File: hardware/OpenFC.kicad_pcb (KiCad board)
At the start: 6 copper layers, 37.5 x 37.5 mm, 167 parts, among them J1 5V, J13 5V, J14 5V, J15 5V, J16 5V, J17 5V, J18 5V, J19 5V, J2 5V, J20 5V, J21 5V, J22 5V, J23 5V, J24 5V, J25 5V, J27 5V, J28 5V, J29 5V, J3 5V, J30 5V, J32 5V, J33 5V, J34 5V, J35 5V, J36 5V, J38 5V, J39 5V, J4 5V, J40 5V, J41 5V, J42 5V, J43 5V, J44 5V, J45 5V, J46 5V, J47 5V, J48 5V, J49 5V, J5 5V, J50 5V, J51 5V, J52 5V, J53 5V, J54 5V, J55 5V, J56 5V, J57 5V, J58 5V, J59 5V, J6 5V, J7 5V, J8 5V, J9 5V, P1 SM08B-SRSS-TB(LF)(SN), Q1 DMN1150UFB-7B, Q2 DMN1150UFB-7B, Q3 DMN1150UFB-7B, Q7 DMN1150UFB-7B, U1 SM06B-SRSS-TB(LF)(SN), U13 LP5912-3.3DRVR, U14 LSM6DSV16XTR, U21 NCV8187AMT180TAG, U32 TS2306A 240GF MSM 9_C2976675, U33 TPS2116DRLR, U34 TLV3201AIDBVR, U35 SN74LVC1G3157DTBR, U36 RP2354B_C39843328, U38 TLV9061IDPWR, U6 LMR51420YFDDCR, U7 LMR51420YFDDCR, X1 XTM25012000JT00351001

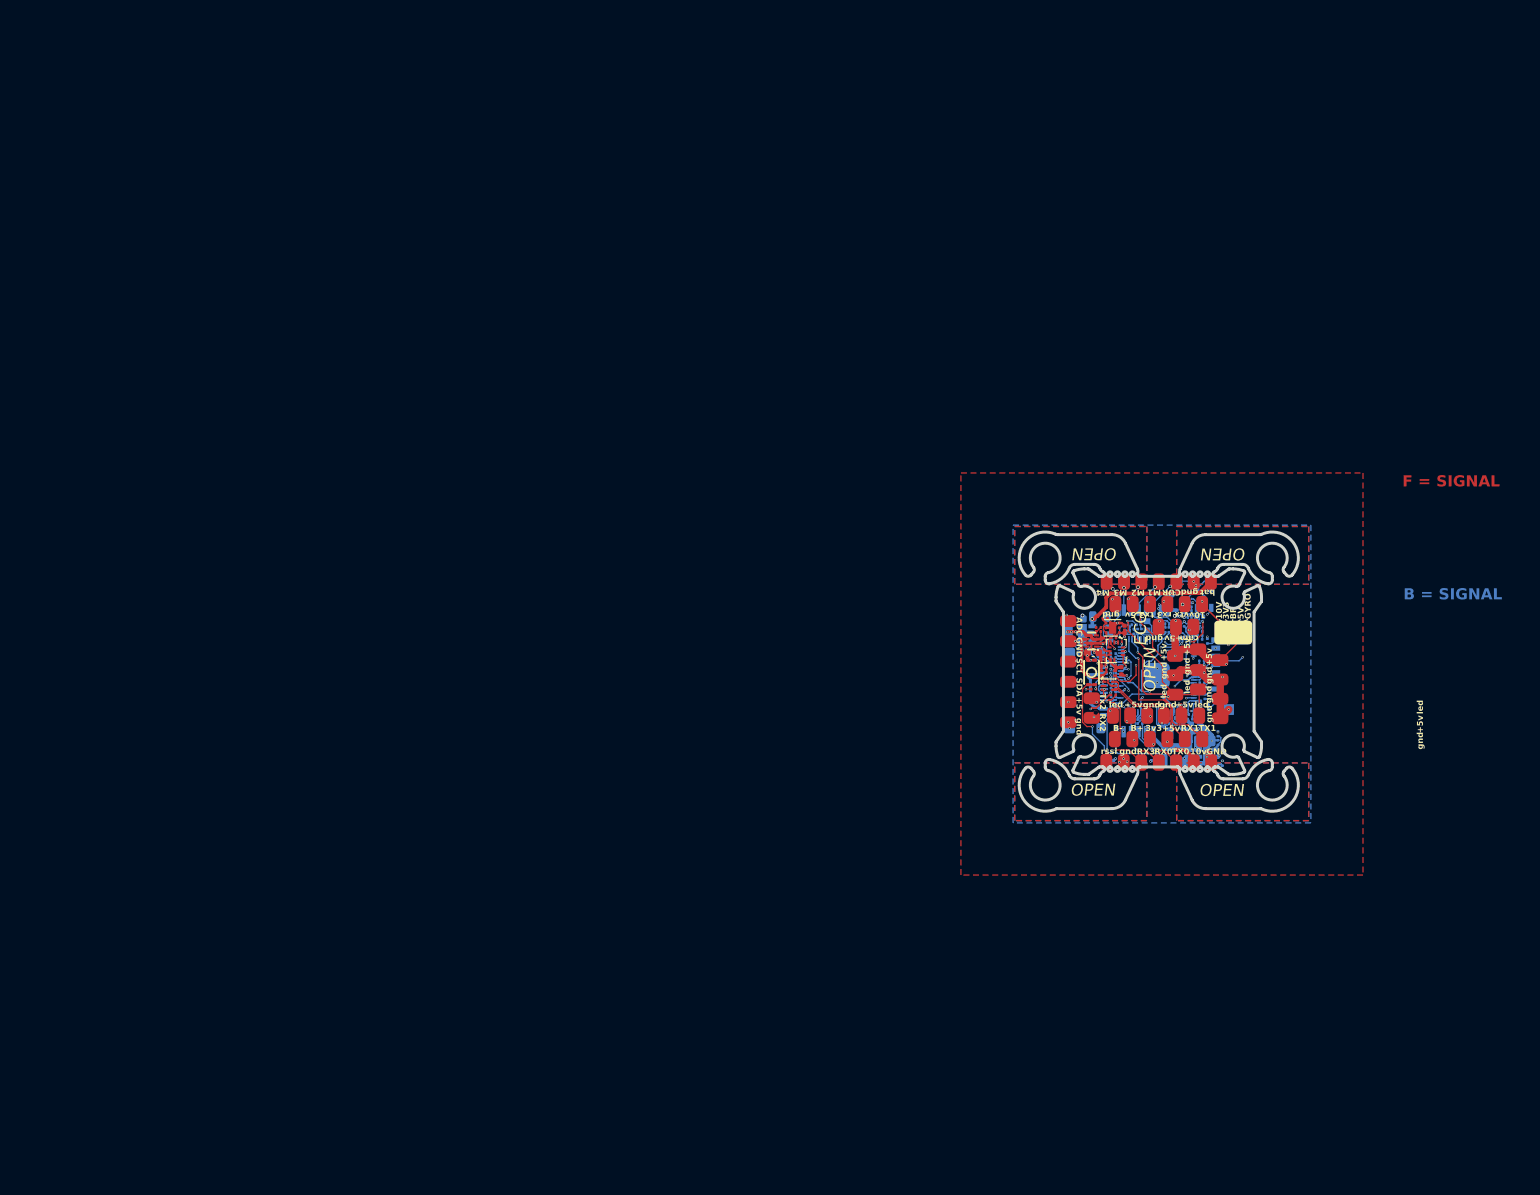
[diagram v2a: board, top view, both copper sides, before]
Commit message: WIP: schematic updates, library modernization, audit tooling
Schematic changes (user):
- Add ADC bypass caps on CURRENT/RSSI/EXTERNAL (1k + 100nF RC filter)
- Add IMU GYRO_CS 10k pull-up to +3.3V
- Reverse P1 ESC 8-pin JST SH pinout to BF standard
  (pin1=V+, pin2=GND, pin3=Current, pin5-8=M1-M4)
- SD card (blackbox) sub-sheet with SPI1 + FLASH_CS + decoupling
- Other sub-sheet cleanup (rp2350a, osd, pads, power, imu)

Footprint library:
- Convert all 62 legacy (module ...) footprints to modern
  (footprint ...) format via pcbnew API — fixes kicad-sch-api
  "footprint not found" errors

Tooling:
- Add hardware/tools/audit_design.py (BF-rule design audit script)
- Add hardware/tools/design_audit.md (audit report output)

Docs:
- Update CLAUDE.md: current GPIO map, corrected power tree net names,
  open issues list (CRIT-2..5), connector verification status

Co-Authored-By: Claude Opus 4.6 (1M context) <noreply@anthropic.com>
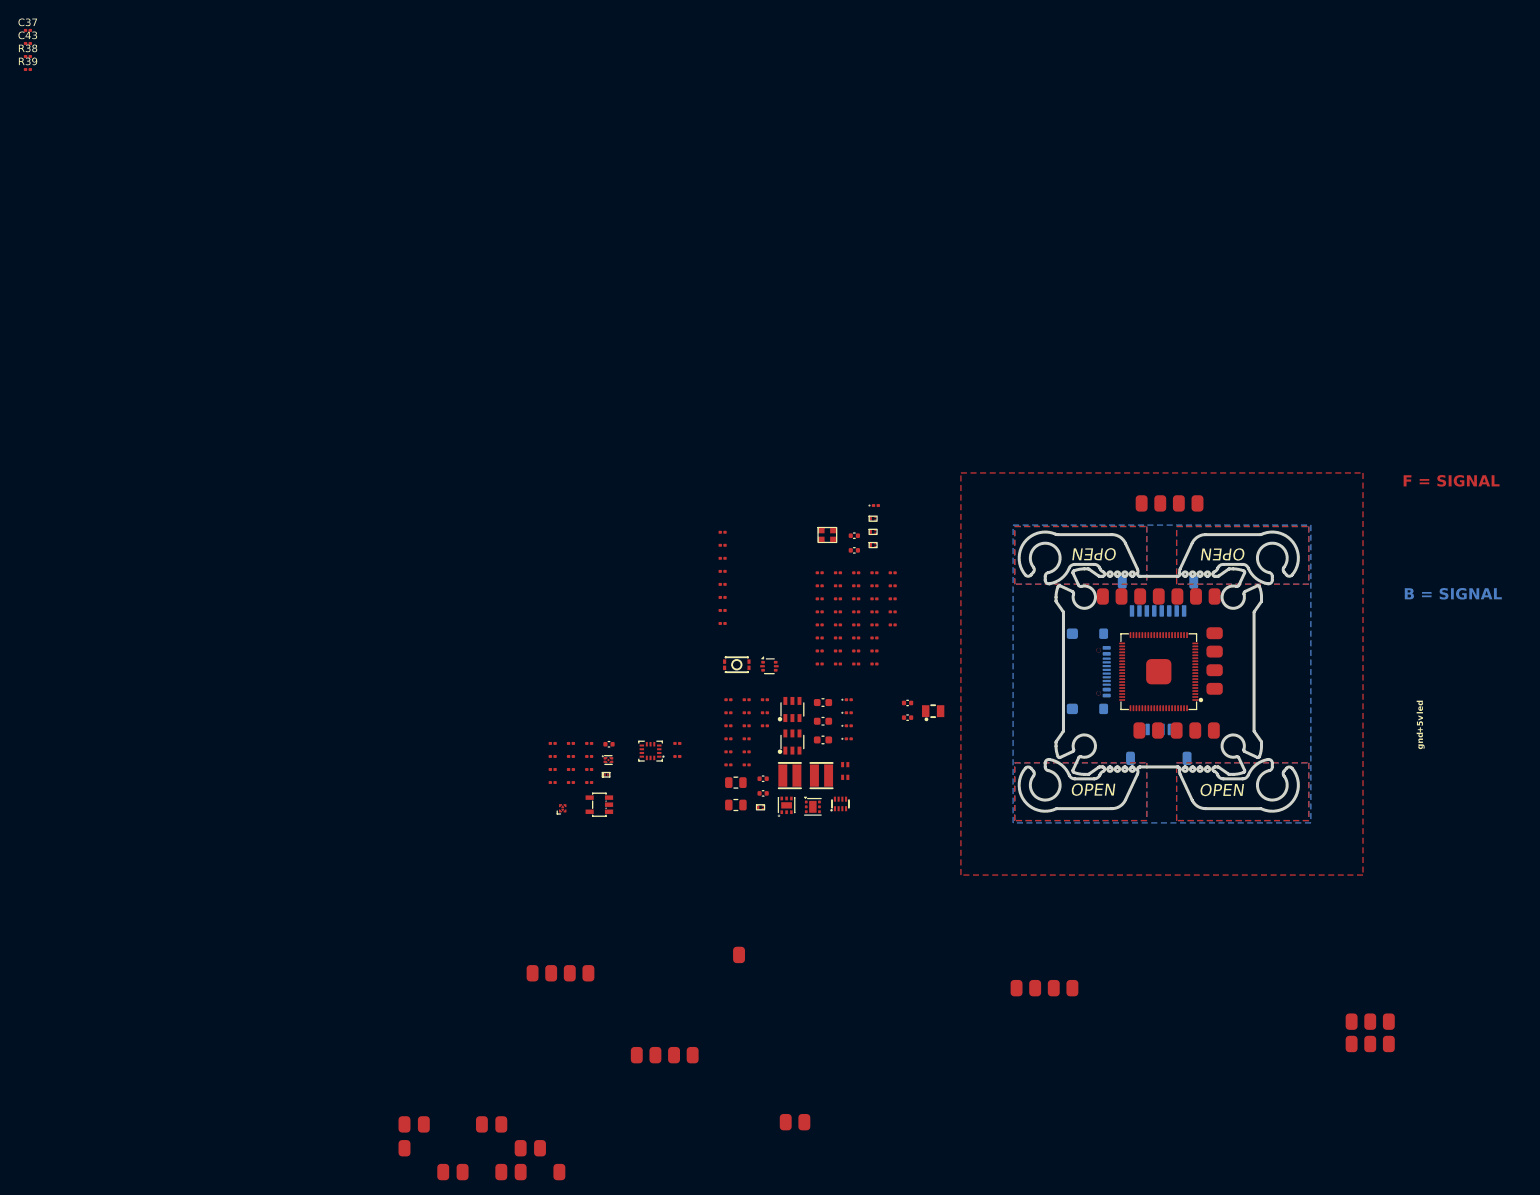
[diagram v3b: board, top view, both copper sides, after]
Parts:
- removed C44, C49, C50, C51, C52, C56, C65, C69: 100n, Capacitor_SMD:C_0201_0603Metric
- removed C48: 22uF, Capacitor_SMD:C_0603_1608Metric
- removed C59, C73: 20p, Capacitor_SMD:C_0201_0603Metric
- removed C60, C62, C67, C68: 4.7uF, Capacitor_SMD:C_0402_1005Metric
- removed C64: 470p, Capacitor_SMD:C_0201_0603Metric
- removed C66: 1uF, Capacitor_SMD:C_0402_1005Metric
- removed Card2: TF-021B-H265, lib:TF-SMD_TF-021B-H265
- removed D21: RB161QS-40_C28646385, lib:SOD-882_L1.0-W0.6-RD
- removed J51, J55, J56, J57, J58, J59: 5V, lib:small_pad
- removed L4: XRTC303020D4R7MBCA, lib:IND-SMD_L3.0-W3.0_AFE303020S
- removed Q7: DMN1150UFB-7B, lib:DFN-3L_L1.0-W0.6-P0.65-BR
- removed R40: 5.1k, Capacitor_SMD:C_0201_0603Metric
- removed R49: 470R, Capacitor_SMD:C_0201_0603Metric
- removed R55: 200R, Capacitor_SMD:C_0201_0603Metric
- removed R56: 30R, Capacitor_SMD:C_0201_0603Metric
- removed U13: LP5912-3.3DRVR, Package_SON:WSON-6-1EP_2x2mm_P0.65mm_EP1x1.6mm
- removed U14: LSM6DSV16XTR, lib:LGA-14_L3.0-W2.5-P0.50-BR
- removed U21: NCV8187AMT180TAG, lib:WDFN-6_L2.0-W2.0-P0.65-BL-EP
- removed U32: TS2306A 240GF MSM 9_C2976675, lib:SW-SMD_4P-L3.0-W2.0-P0.85-LS3.5
- removed U33: TPS2116DRLR, lib:SOT-583-8_L2.1-W1.6-P0.50-LS1.6-BL
- removed U34: TLV3201AIDBVR, lib:SOT-23-5_L3.0-W1.7-P0.95-LS2.8-BR
- removed U35: SN74LVC1G3157DTBR, lib:X2SON-6_L1.0-W0.8-BL
- removed U36: RP2354B_C39843328, lib:QFN-80_L10.0-W10.0-P0.40-TL-EP3.4
- removed U38: TLV9061IDPWR, lib:X2SON-4_L0.8-W0.8-P0.48-TL-DPW
- added C10: 20p, Capacitor_SMD:C_0201_0603Metric, F.Cu at (109.5, 73.2)
- added C11: 100n, Capacitor_SMD:C_0201_0603Metric, F.Cu at (109.5, 75.0)
- added C12: 100n, Capacitor_SMD:C_0201_0603Metric, F.Cu at (109.5, 76.7)
- added C13: 100n, Capacitor_SMD:C_0201_0603Metric, F.Cu at (109.5, 78.5)
- added C14: 100n, Capacitor_SMD:C_0201_0603Metric, F.Cu at (94.0, 67.8)
- added C15: 100n, Capacitor_SMD:C_0201_0603Metric, F.Cu at (94.0, 69.5)
- added C17: 100n, Capacitor_SMD:C_0201_0603Metric, F.Cu at (109.5, 80.2)
- added C18: 4.7uF, Capacitor_SMD:C_0402_1005Metric, F.Cu at (118.9, 92.7)
- added C19: 100n, Capacitor_SMD:C_0201_0603Metric, F.Cu at (109.5, 83.7)
- added C20: 4.7uF, Capacitor_SMD:C_0402_1005Metric, F.Cu at (118.9, 90.7)
- added C21: 4.7uF, Capacitor_SMD:C_0402_1005Metric, F.Cu at (111.7, 68.2)
- added C22: 100n, Capacitor_SMD:C_0201_0603Metric, F.Cu at (94.0, 73.0)
- added C23: 4.7uF, Capacitor_SMD:C_0402_1005Metric, F.Cu at (111.7, 70.2)
- added C24: 4.7uF 50v, Capacitor_SMD:C_0805_2012Metric, F.Cu at (95.8, 101.4)
- added C25: 4.7uF 50v, Capacitor_SMD:C_0805_2012Metric, F.Cu at (95.8, 104.4)
- added C26: 100n, Capacitor_SMD:C_0201_0603Metric, F.Cu at (94.8, 90.3)
- added C4: 100n, Capacitor_SMD:C_0201_0603Metric, F.Cu at (109.5, 82.0)
- added C5: 100n, Capacitor_SMD:C_0201_0603Metric, F.Cu at (107.1, 78.5)
- added C6: 20p, Capacitor_SMD:C_0201_0603Metric, F.Cu at (107.1, 80.2)
- added C7: 100n, Capacitor_SMD:C_0201_0603Metric, F.Cu at (107.1, 82.0)
- added C8: 100n, Capacitor_SMD:C_0201_0603Metric, F.Cu at (107.1, 83.7)
- added C9: 100n, Capacitor_SMD:C_0201_0603Metric, F.Cu at (107.1, 85.5)
- added D6: RB161QS-40_C28646385, lib:SOD-882_L1.0-W0.6-RD, F.Cu at (110.5, 100.7)
- added J10: 5V, lib:small_pad, F.Cu at (51.3, 150.5)
- added J11: 5V, lib:small_pad, F.Cu at (82.5, 138.0)
- added J12: 5V, lib:small_pad, F.Cu at (68.5, 127.0)
- added J26: 5V, lib:small_pad, F.Cu at (160.1, 83.8)
- added J31: 5V, lib:small_pad, F.Cu at (147.6, 76.4)
- added J37: 5V, lib:small_pad, F.Cu at (155.1, 76.4)
- added L2: XRTC303020D4R7MBCA, lib:IND-SMD_L3.0-W3.0_AFE303020S, F.Cu at (103.1, 100.5)
- added Q4: DMN1150UFB-7B, lib:DFN-3L_L1.0-W0.6-P0.65-BR, F.Cu at (99.1, 104.7)
- added R10: 10k, Capacitor_SMD:C_0201_0603Metric, F.Cu at (114.4, 73.2)
- added R18: 2.2k, Capacitor_SMD:C_0201_0603Metric, F.Cu at (114.4, 80.2)
- added R24: 10k, Capacitor_SMD:C_0201_0603Metric, F.Cu at (116.9, 76.7)
- added R25: 2.2k, Capacitor_SMD:C_0201_0603Metric, F.Cu at (116.9, 78.5)
- added R26: 200R, Capacitor_SMD:C_0201_0603Metric, F.Cu at (116.9, 80.2)
- added R32: 13.7k, Capacitor_SMD:C_0201_0603Metric, F.Cu at (97.3, 95.5)
- added R33: 470R, Capacitor_SMD:C_0201_0603Metric, F.Cu at (97.3, 97.3)
- added U18: SN74LVC1G3157DTBR, lib:X2SON-6_L1.0-W0.8-BL, F.Cu at (72.5, 104.8)
- added U19: TLV9061IDPWR, lib:X2SON-4_L0.8-W0.8-P0.48-TL-DPW, F.Cu at (78.7, 98.4)
- added U2: RP2354B_C39843328, lib:QFN-80_L10.0-W10.0-P0.40-TL-EP3.4, F.Cu at (152.6, 86.5)
- added U20: TLV3201AIDBVR, lib:SOT-23-5_L3.0-W1.7-P0.95-LS2.8-BR, F.Cu at (77.5, 104.4)
- added U3: LMR51420YFDDCR, lib:SOT-23-6_L2.9-W1.6-P0.95-LS2.9-BL, F.Cu at (103.4, 91.6)
- added U4: LMR51420YFDDCR, lib:SOT-23-6_L2.9-W1.6-P0.95-LS2.9-BL, F.Cu at (103.4, 95.9)
- added U5: TPS2116DRLR, lib:SOT-583-8_L2.1-W1.6-P0.50-LS1.6-BL, F.Cu at (109.9, 104.3)
- added U8: SM06B-SRSS-TB(LF)(SN), lib:CONN-SMD_SM06B-SRSS-TB-LF-SN, B.Cu at (152.6, 96.2)
- added U9: LSM6DSV16XTR, lib:LGA-14_L3.0-W2.5-P0.50-BR, F.Cu at (84.3, 97.2)
- C1, C27, C3, C31, C36, C39, C42, C43, D9, L1, L3, Q2, Q3, R2, R34, R35, X1: moved to F.Cu
- C16, C2: value 22uF -> 100n; footprint Capacitor_SMD:C_0402_1005Metric -> Capacitor_SMD:C_0201_0603Metric
- C28, C29, C30: value 100n -> 22uF; footprint Capacitor_SMD:C_0201_0603Metric -> Capacitor_SMD:C_0603_1608Metric; moved to F.Cu
- C33, C34: value 100n -> 22uF; footprint Capacitor_SMD:C_0201_0603Metric -> Capacitor_SMD:C_0402_1005Metric
- C35, C37: value 4.7uF 50v -> 100n; footprint Capacitor_SMD:C_0805_2012Metric -> Capacitor_SMD:C_0201_0603Metric; moved to F.Cu
- C38: value 22uF -> 470p; footprint Capacitor_SMD:C_0603_1608Metric -> Capacitor_SMD:C_0201_0603Metric; moved to F.Cu
- C40: value 22uF -> 1uF; footprint Capacitor_SMD:C_0603_1608Metric -> Capacitor_SMD:C_0402_1005Metric; moved to F.Cu
- D1: value LED_1_Green -> USBLC6-2P6; footprint LED_SMD:LED_0201_0603Metric -> Package_TO_SOT_SMD:SOT-666
- D8: value USBLC6-2P6 -> LED_1_Green; footprint Package_TO_SOT_SMD:SOT-666 -> LED_SMD:LED_0201_0603Metric
- R1: value 10k -> 100k; moved to F.Cu
- R11: value 1k -> 10k; moved to F.Cu
- R12: value 200R -> 30R
- R13: value 1k -> 30R; moved to F.Cu
- R14, R16: value 100k -> 30R; moved to F.Cu
- R15: value 200R -> 10k
- R17: value 100k -> 2.2k; moved to F.Cu
- R19: value 10k -> 1k
- R20: value 10k -> 1k; moved to F.Cu
- R21: value 75R -> 100k; moved to F.Cu
- R22: value 30R -> 2.2k; moved to F.Cu
- R23: value 1k -> 100k; moved to F.Cu
- R27: value 680R -> 100k; moved to F.Cu
- R28: value 6.8k -> 39k; moved to F.Cu
- R29: value 470R -> 100k
- R3: value 10k -> 5.1k; moved to F.Cu
- R30: value 3.9k -> 6.8k; moved to F.Cu
- R31: value 13.7k -> 100k; moved to F.Cu
- R36: value 10k -> 30R; moved to F.Cu
- R37: value 30R -> 200R; moved to F.Cu
- R38: value 30R -> 10k; moved to F.Cu
- R39: value 5.1k -> 10k
- R4: value 30R -> 5.1k
- R41: value 2.2k -> 75R; moved to F.Cu
- R42: value 2.2k -> 3.9k; moved to F.Cu
- R43: value 100k -> 12k; moved to F.Cu
- R44: value 10k -> 1.4k; moved to F.Cu
- R45: value 1.4k -> 680R; moved to F.Cu
- R46: value 12k -> 470R; moved to F.Cu
- R47: value 75R -> 470R; moved to F.Cu
- R48: value 470R -> 75R; moved to F.Cu
- R5: value 100k -> 1k; moved to F.Cu
- R6: value 2.2k -> 1k; moved to F.Cu
- R7: value 100k -> 1k
- R8: value 39k -> 1k
- R9: value 2.2k -> 200R; moved to F.Cu
- U1: value SM06B-SRSS-TB(LF)(SN) -> TS2306A 240GF MSM 9_C2976675; footprint lib:CONN-SMD_SM06B-SRSS-TB-LF-SN -> lib:SW-SMD_4P-L3.0-W2.0-P0.85-LS3.5; moved to F.Cu
- U6: value LMR51420YFDDCR -> NCV8187AMT180TAG; footprint lib:SOT-23-6_L2.9-W1.6-P0.95-LS2.9-BL -> lib:WDFN-6_L2.0-W2.0-P0.65-BL-EP; moved to F.Cu
- U7: value LMR51420YFDDCR -> LP5912-3.3DRVR; footprint lib:SOT-23-6_L2.9-W1.6-P0.95-LS2.9-BL -> Package_SON:WSON-6-1EP_2x2mm_P0.65mm_EP1x1.6mm; moved to F.Cu
- moved R38 177.0 mm to (0.72, 3.88), turned to 0 degrees
- moved C43 169.8 mm to (0.72, 2.12), turned to 0 degrees
- moved R39 165.6 mm to (0.72, 5.62)
- moved C37 164.1 mm to (0.72, 0.38)
- moved J3 124.0 mm to (56.5, 153.7)
- moved J4 123.2 mm to (59.1, 153.7)
- moved J24 116.3 mm to (64.3, 147.3)
- moved J19 111.9 mm to (51.3, 147.3)
- moved J20 111.6 mm to (53.9, 147.3)
- moved J16 110.0 mm to (66.9, 150.5), turned to 90 degrees
- moved J23 106.8 mm to (61.7, 147.3)
- moved J17 106.4 mm to (69.5, 150.5), turned to 90 degrees
- moved J6 98.9 mm to (64.3, 153.7), turned to 90 degrees
- moved J7 98.7 mm to (66.9, 153.7), turned to 90 degrees
- moved J14 93.7 mm to (73.5, 127.0), turned to 90 degrees
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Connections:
- C1 pad 1: +3.3V -> +1.1V
- C16 pad 1: +3.3V -> GND
- C16 pad 2: GND -> /PADS/ADC2
- C2 pad 1: +1.8V_GYRO -> +1.1V
- C27 pad 1: +1.1V -> Net-(U4-SW)
- C27 pad 2: GND -> Net-(U4-CB)
- C28 pad 1: +1.1V -> +10V
- C29 pad 1: +1.1V -> +5V_BUCK
- C3 pad 1: +3.3V -> +1.1V
- C30 pad 1: +3.3V -> +5V
- C31 pad 1: +3.3V -> +5V
- C33 pad 1: +5V -> +1.8V_GYRO
- C35 pad 1: +BATT -> +1.8V_GYRO
- C36 pad 1: Net-(U6-SW) -> +3.3V
- C36 pad 2: Net-(U6-CB) -> GND
- C37 pad 1: +BATT -> unconnected-(C37-Pad1)
- C37 pad 2: GND -> unconnected-(C37-Pad2)
- C38 pad 1: +10V -> /OSD/VID_FILT
- C39 pad 1: Net-(U7-SW) -> +3.3V
- C39 pad 2: Net-(U7-CB) -> GND
- C40 pad 1: +5V_BUCK -> /OSD/VID_FILT
- C40 pad 2: GND -> /OSD/VID_DC
- C41 pad 1: +1.8V_GYRO -> +3.3V
- D1 pad 1: GND -> /RP2350A/D+_C
- D1 pad 2: Net-(D1-A) -> GND
- D7 pad 1: Net-(D7-K) -> GND
- D8 pad 1: /RP2350A/D+_C -> Net-(D8-K)
- D8 pad 2: GND -> Net-(D8-A)
- J1 pad 1: /PADS/M4 -> GND
- J13 pad 1: +5V -> GND
- J15 pad 1: /LED -> /I2C_SCL
- J17 pad 1: GND -> +5V
- J18 pad 1: /LED -> /I2C_SDA
- J19 pad 1: +5V -> GND
- J2 pad 1: /PADS/M3 -> /PADS/RSSI
- J21 pad 1: /LED -> /PADS/BUZZER-
- J23 pad 1: GND -> /LED
- J24 pad 1: /PADS/CURRENT -> /LED
- J25 pad 1: GND -> +5V
- J27 pad 1: +BATT -> GND
- J28 pad 1: +10V -> +3.3V
- J29 pad 1: GND -> +BATT
- J3 pad 1: /PADS/M2 -> +5V
- J30 pad 1: /LED -> +5V
- J33 pad 1: /OSD/VIDEO_OUT -> /PADS/CURRENT
- J34 pad 1: +5V -> /OSD/VIDEO_OUT
- J35 pad 1: /PADS/DIGITAL_TX -> /PADS/M1
- J36 pad 1: /PADS/DIGITAL_RX -> GND
- J38 pad 1: /PADS/SBUS -> +10V
- J39 pad 1: +5V -> /PADS/M3
- J4 pad 1: /PADS/M1 -> +5V
- J40 pad 1: /PADS/BUZZER- -> +5V
- J41 pad 1: GND -> /PADS/M4
- J43 pad 1: /UART1_TX -> /PADS/PIOUART0_TX
- J44 pad 1: /UART1_RX -> /PADS/PIOUART0_RX
- J45 pad 1: /PADS/PIOUART0_RX -> +10V
- J46 pad 1: /PADS/PIOUART0_TX -> GND
- J47 pad 1: GND -> +5V
- J48 pad 1: +5V -> /PADS/DIGITAL_TX
- J49 pad 1: +5V -> /PADS/DIGITAL_RX
- J5 pad 1: GND -> +5V
- J52 pad 1: /PADS/ADC2 -> /PADS/PIOUART1_TX
- J53 pad 1: +5V -> /PADS/SBUS
- J54 pad 1: GND -> /PADS/PIOUART1_RX
- J6 pad 1: +5V -> GND
- J7 pad 1: /I2C_SDA -> GND
- J8 pad 1: /I2C_SCL -> /UART1_RX
- J9 pad 1: GND -> /LED
- L3 pad 1: Net-(U6-SW) -> Net-(U4-SW)
- L3 pad 2: +10V -> +5V_BUCK
- P1 pad 1: /PADS/M4 -> +BATT
- P1 pad 2: /PADS/M3 -> GND
- P1 pad 3: /PADS/M2 -> /PADS/CURRENT
- P1 pad 4: /PADS/M1 -> unconnected-(P1-Pad4)
- P1 pad 5: unconnected-(P1-Pad5) -> /PADS/M1
- P1 pad 6: /PADS/CURRENT -> /PADS/M2
- P1 pad 7: GND -> /PADS/M3
- P1 pad 8: +BATT -> /PADS/M4
- Q1 pad 1: /POWER/1.8V_PG -> Net-(Q1-G)
- Q1 pad 3: Net-(D7-K) -> /RP2350A/SBUS_INVERT
- Q2 pad 3: /RP2350A/SBUS_INVERT -> /PADS/BUZZER-
- R1 pad 1: Net-(Card2-DAT2) -> +BATT
- R1 pad 2: +3.3V -> /RP2350A/ADC_VBAT
- R11 pad 1: Net-(Q2-G) -> Net-(R11-Pad1)
- R11 pad 2: /PADS/SBUS -> Net-(U2-QSPI_SS)
- R12 pad 1: +5V -> /RP2350A/D-
- R12 pad 2: Net-(D7-A) -> Net-(U2-USB_DM)
- R13 pad 1: Net-(Q7-G) -> Net-(U2-USB_DP)
- R13 pad 2: /RP2350A/BEEPER -> /RP2350A/D+
- R14 pad 1: Net-(U6-FB) -> +3.3V
- R14 pad 2: +10V -> Net-(U2-VREG_AVDD)
- R15 pad 1: +5V_BUCK -> unconnected-(R15-Pad1)
- R15 pad 2: Net-(D1-A) -> +3.3V
- R16 pad 1: Net-(U7-FB) -> /RP2350A/LED0
- R16 pad 2: +5V_BUCK -> Net-(D2-A)
- R17 pad 1: GND -> +3.3V
- R17 pad 2: Net-(Q2-G) -> /I2C_SCL
- R19 pad 1: /POWER/1.8V_PG -> Net-(Q1-G)
- R19 pad 2: +5V -> /PADS/SBUS
- R2 pad 1: /BLACKBOX/BB_CS -> GND
- R2 pad 2: +3.3V -> /RP2350A/ADC_VBAT
- R20 pad 1: /RP2350A/SBUS_INVERT -> Net-(Q2-G)
- R20 pad 2: +3.3V -> /RP2350A/BEEPER
- R21 pad 1: /OSD/VIDEO_IN -> GND
- R21 pad 2: GND -> Net-(Q1-G)
- R22 pad 1: /RP2350A/LED0 -> +3.3V
- R22 pad 2: Net-(D2-A) -> /RP2350A/LED_STRIP_L
- R23 pad 1: /RP2350A/XOUT -> GND
- R23 pad 2: Net-(C73-Pad2) -> Net-(Q2-G)
- R27 pad 1: /OSD/VID_FILT -> Net-(U5-PR1)
- R27 pad 2: /OSD/VIDEO_IN -> +5V_BUCK
- R28 pad 1: Net-(U6-FB) -> Net-(U5-PR1)
- R29 pad 1: +10V -> Net-(U3-FB)
- R29 pad 2: Net-(D5-A) -> +10V
- R3 pad 1: Net-(Card2-DAT1) -> GND
- R3 pad 2: +3.3V -> Net-(USB1-CC1)
- R30 pad 1: /OSD/OSD_W -> Net-(U3-FB)
- R30 pad 2: /OSD/OSD_LVL -> GND
- R31 pad 1: Net-(U7-FB) -> Net-(U4-FB)
- R31 pad 2: GND -> +5V_BUCK
- R34 pad 1: Net-(Q3-D) -> +5V_BUCK
- R34 pad 2: /LED -> Net-(D5-A)
- R35 pad 1: GND -> /POWER/1.8V_PG
- R35 pad 2: /RP2350A/ADC_VBAT -> +5V
- R36 pad 2: Net-(U36-RUN) -> Net-(D7-A)
- R37 pad 1: /RP2350A/D- -> +5V
- R37 pad 2: Net-(U36-USB_DM) -> Net-(D8-A)
- R38 pad 1: Net-(U36-USB_DP) -> unconnected-(R38-Pad1)
- R38 pad 2: /RP2350A/D+ -> unconnected-(R38-Pad2)
- R39 pad 1: GND -> unconnected-(R39-Pad1)
- R39 pad 2: Net-(USB1-CC2) -> unconnected-(R39-Pad2)
- R4 pad 1: +3.3V -> GND
- R4 pad 2: Net-(D4-A) -> Net-(USB1-CC2)
- R41 pad 1: +3.3V -> /OSD/VIDEO_IN
- R41 pad 2: /I2C_SCL -> GND
- R42 pad 1: /I2C_SDA -> /OSD/OSD_W
- R42 pad 2: +3.3V -> /OSD/OSD_LVL
- R43 pad 1: +BATT -> /OSD/OSD_LVL
- R43 pad 2: /RP2350A/ADC_VBAT -> +3.3V
- R44 pad 1: Net-(R44-Pad1) -> GND
- R44 pad 2: Net-(U36-QSPI_SS) -> /OSD/OSD_LVL
- R45 pad 1: GND -> /OSD/VID_FILT
- R45 pad 2: /OSD/OSD_LVL -> /OSD/VIDEO_IN
- R46 pad 1: /OSD/OSD_LVL -> GND
- R46 pad 2: +3.3V -> Net-(U19-IN-)
- R47 pad 1: Net-(U38-OUT) -> Net-(U19-IN-)
- R47 pad 2: /OSD/VIDEO_OUT -> Net-(U19-OUT)
- R48 pad 1: GND -> Net-(U19-OUT)
- R48 pad 2: Net-(U38-IN-) -> /OSD/VIDEO_OUT
- R5 pad 1: GND -> /RP2350A/XOUT
- R5 pad 2: Net-(Q7-G) -> Net-(C10-Pad2)
- R6 pad 1: +3.3V -> Net-(U2-GPIO40_ADC0)
- R6 pad 2: /RP2350A/LED_STRIP_L -> /PADS/CURRENT
- R7 pad 1: Net-(U33-PR1) -> Net-(U2-GPIO45_ADC5)
- R7 pad 2: +5V_BUCK -> /PADS/RSSI
- R8 pad 1: Net-(U33-PR1) -> Net-(U2-GPIO47_ADC7)
- R8 pad 2: GND -> /PADS/ADC2
- R9 pad 1: +5V -> +3.3V
- R9 pad 2: Net-(Q3-D) -> Net-(U2-ADC_AVDD)
- U1 pad 1: +10V -> GND
- U1 pad 2: GND -> Net-(R11-Pad1)
- U6 pad 1: GND -> +5V
- U6 pad 2: Net-(U6-SW) -> +5V
- U6 pad 3: +BATT -> GND
- U6 pad 4: Net-(U6-FB) -> /POWER/1.8V_PG
- U6 pad 5: /POWER/10V_ENABLE -> +1.8V_GYRO
- U6 pad 6: Net-(U6-CB) -> +1.8V_GYRO
- U7 pad 1: GND -> +3.3V
- U7 pad 2: Net-(U7-SW) -> unconnected-(U7-NC-Pad2)
- U7 pad 3: +BATT -> GND
- U7 pad 4: Net-(U7-FB) -> +5V
- U7 pad 5: +BATT -> GND
- U7 pad 6: Net-(U7-CB) -> +5V
- X1 pad 3: Net-(C73-Pad2) -> Net-(C10-Pad2)
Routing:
- net GND: track 95.7 -> 0.00 mm, vias 57 -> 0
- net +3.3V: track 78.4 -> 0.00 mm, vias 18 -> 0
- net +BATT: track 74.3 -> 0.00 mm, vias 7 -> 0
- net +5V_BUCK: track 39.6 -> 0.00 mm, vias 4 -> 0
- net +10V: track 39.2 -> 0.00 mm, vias 7 -> 0
- net +5V: track 34.7 -> 0.00 mm, vias 12 -> 0
- net /LED: track 31.0 -> 0.00 mm, vias 3 -> 0
- net +1.1V: track 30.5 -> 0.00 mm, vias 3 -> 0
- net /PADS/ADC2: track 28.2 -> 0.00 mm, vias 2 -> 0
- net /POWER/1.8V_PG: track 27.7 -> 0.00 mm, vias 2 -> 0
- net Net-(R44-Pad1): track 25.6 -> 0.00 mm, vias 1 -> 0
- net /PADS/SBUS: track 24.3 -> 0.00 mm, vias 2 -> 0
- net /PADS/M4: track 22.4 -> 0.00 mm, vias 2 -> 0
- net /PADS/M3: track 20.3 -> 0.00 mm, vias 2 -> 0
- net /UART1_TX: track 19.8 -> 0.00 mm, vias 1 -> 0
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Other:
- board text removed: "10V"
- board text removed: "10v"
- board text removed: "3V3"
- board text removed: "3v3"
- board text removed: "5V"
- board text removed: "5v"
- board text removed: "ADC"
- board text removed: "B+"
- board text removed: "B-"
- board text removed: "BF"
- board text removed: "CUR"
- board text removed: "ECO"
- board text removed: "GND"
- board text removed: "GYRO"
- board text removed: "M1"
- board text removed: "M2"
- board text removed: "M3"
- board text removed: "M4"
- board text removed: "RX0"
- board text removed: "RX1"
- board text removed: "RX2"
- board text removed: "RX3"
- board text removed: "SCL"
- board text removed: "SDA"
- board text removed: "TX0"
- board text removed: "TX1"
- board text removed: "Tx2"
- board text removed: "bat"
- board text removed: "cam"
- board text removed: "rssi"
- board text removed: "rx3"
- board text removed: "tx3"
- board text removed: "vtx"
